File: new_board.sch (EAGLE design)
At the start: 22 parts, among them J4 455-1750-1-ND, Q1 BD437

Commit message: added analog/digital switch
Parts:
- added S4: MOMENTARY-SWITCH-SPST-SMD-RIGHT-ANGLE, SparkFun-Switches:MOMENTARY-SWITCH-SPST-SMD-RIGHT-ANGLE
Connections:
- net N$16: now also S4.1
- net N$6: now also S4.2
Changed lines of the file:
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@@
 </part>
 <part name="GND8" library="SparkFun-PowerSymbols" deviceset="GND" device=""/>
+<part name="S4" library="SparkFun-Switches" deviceset="MOMENTARY-SWITCH-SPST" device="-SMD-RIGHT-ANGLE">
+<attribute name="PROD_ID" value="Analog/Digital"/>
+</part>
 </parts>
 <sheets>
@@
 <instance part="GND8" gate="1" x="160.02" y="124.46" smashed="yes">
 <attribute name="VALUE" x="160.02" y="124.206" size="1.778" layer="96" align="top-center"/>
+</instance>
+<instance part="S4" gate="G$1" x="266.7" y="60.96" smashed="yes" rot="R90">
+<attribute name="PROD_ID" x="264.16" y="53.34" size="1.778" layer="96" rot="R90"/>
 </instance>
 </instances>
@@
 <wire x1="182.88" y1="81.28" x2="180.34" y2="81.28" width="0.1524" layer="91"/>
 <junction x="182.88" y="81.28"/>
+<pinref part="S4" gate="G$1" pin="2"/>
+<wire x1="266.7" y1="81.28" x2="266.7" y2="66.04" width="0.1524" layer="91"/>
 </segment>
 </net>
@@
 <junction x="149.86" y="76.2"/>
 <pinref part="S5" gate="G$1" pin="1"/>
-<wire x1="254" y1="20.32" x2="279.4" y2="20.32" width="0.1524" layer="91"/>
+<wire x1="254" y1="20.32" x2="266.7" y2="20.32" width="0.1524" layer="91"/>
+<wire x1="266.7" y1="20.32" x2="279.4" y2="20.32" width="0.1524" layer="91"/>
 <wire x1="279.4" y1="20.32" x2="279.4" y2="55.88" width="0.1524" layer="91"/>
 <pinref part="J4" gate="J$1" pin="3"/>
@@
 <wire x1="106.68" y1="114.3" x2="106.68" y2="76.2" width="0.1524" layer="91"/>
 <pinref part="R7" gate="G$1" pin="2"/>
-<wire x1="109.22" y1="5.08" x2="116.84" y2="5.08" width="0.1524" layer="91"/>
+<wire x1="106.68" y1="5.08" x2="116.84" y2="5.08" width="0.1524" layer="91"/>
 <wire x1="116.84" y1="5.08" x2="119.38" y2="5.08" width="0.1524" layer="91"/>
 <junction x="116.84" y="5.08"/>
 <wire x1="106.68" y1="20.32" x2="106.68" y2="5.08" width="0.1524" layer="91"/>
-<wire x1="106.68" y1="5.08" x2="109.22" y2="5.08" width="0.1524" layer="91"/>
-</segment>
-</net>
+<pinref part="S4" gate="G$1" pin="1"/>
+<wire x1="266.7" y1="55.88" x2="266.7" y2="20.32" width="0.1524" layer="91"/>
+</segment>
+</net>

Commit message: routing PCB layout
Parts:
- J2: 9V_BATTERY (none) -> 9V
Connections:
- removed net N$14: J2.2
- net GND: now also J2.2
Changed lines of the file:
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@@
 </part>
 <part name="J2" library="SparkFun-Connectors" deviceset="CONN_02" device="">
-<attribute name="9V_BATTERY" value=""/>
+<attribute name="9V_BATTERY" value="9V"/>
 </part>
 <part name="S1" library="SparkFun-Switches" deviceset="MOMENTARY-SWITCH-SPST" device="-SMD-RIGHT-ANGLE">
@@
 <attribute name="PROD_ID" value="Motor Button"/>
 </part>
-<part name="GND5" library="SparkFun-PowerSymbols" deviceset="GND" device=""/>
 <part name="J3" library="SparkFun-Connectors" deviceset="CONN_02" device="">
 <attribute name="TEAM_BATTERY" value=""/>
@@
 <instance part="S3" gate="G$1" x="269.24" y="124.46" smashed="yes" rot="R90">
 <attribute name="PROD_ID" x="266.7" y="121.92" size="1.778" layer="96" rot="R90"/>
-</instance>
-<instance part="GND5" gate="1" x="129.54" y="33.02" smashed="yes">
-<attribute name="VALUE" x="129.54" y="32.766" size="1.778" layer="96" align="top-center"/>
 </instance>
 <instance part="J3" gate="G$1" x="269.24" y="142.24" smashed="yes" rot="R270">
@@
 </segment>
 <segment>
-<pinref part="U$1" gate="G$1" pin="GND"/>
-<pinref part="GND3" gate="1" pin="GND"/>
-<wire x1="149.86" y1="71.12" x2="137.16" y2="71.12" width="0.1524" layer="91"/>
-<wire x1="137.16" y1="71.12" x2="137.16" y2="68.58" width="0.1524" layer="91"/>
-</segment>
-<segment>
 <pinref part="D5" gate="D1" pin="C"/>
 <pinref part="GND2" gate="1" pin="GND"/>
@@
 <pinref part="GND7" gate="1" pin="GND"/>
 <wire x1="139.7" y1="5.08" x2="147.32" y2="5.08" width="0.1524" layer="91"/>
+</segment>
+<segment>
+<pinref part="J2" gate="G$1" pin="2"/>
+<pinref part="U$1" gate="G$1" pin="GND"/>
+<pinref part="GND3" gate="1" pin="GND"/>
+<wire x1="149.86" y1="71.12" x2="139.7" y2="71.12" width="0.1524" layer="91"/>
+<wire x1="139.7" y1="71.12" x2="137.16" y2="71.12" width="0.1524" layer="91"/>
+<wire x1="137.16" y1="71.12" x2="137.16" y2="68.58" width="0.1524" layer="91"/>
+<wire x1="139.7" y1="38.1" x2="139.7" y2="71.12" width="0.1524" layer="91"/>
 </segment>
 </net>
@@
 </segment>
 </net>
-<net name="N$14" class="0">
-<segment>
-<pinref part="J2" gate="G$1" pin="2"/>
-<wire x1="139.7" y1="38.1" x2="139.7" y2="40.64" width="0.1524" layer="91"/>
-<wire x1="139.7" y1="40.64" x2="129.54" y2="40.64" width="0.1524" layer="91"/>
-<wire x1="129.54" y1="40.64" x2="129.54" y2="35.56" width="0.1524" layer="91"/>
-<pinref part="GND5" gate="1" pin="GND"/>
-<wire x1="129.54" y1="35.56" x2="129.54" y2="33.02" width="0.1524" layer="91"/>
-<junction x="129.54" y="35.56"/>
-</segment>
-</net>

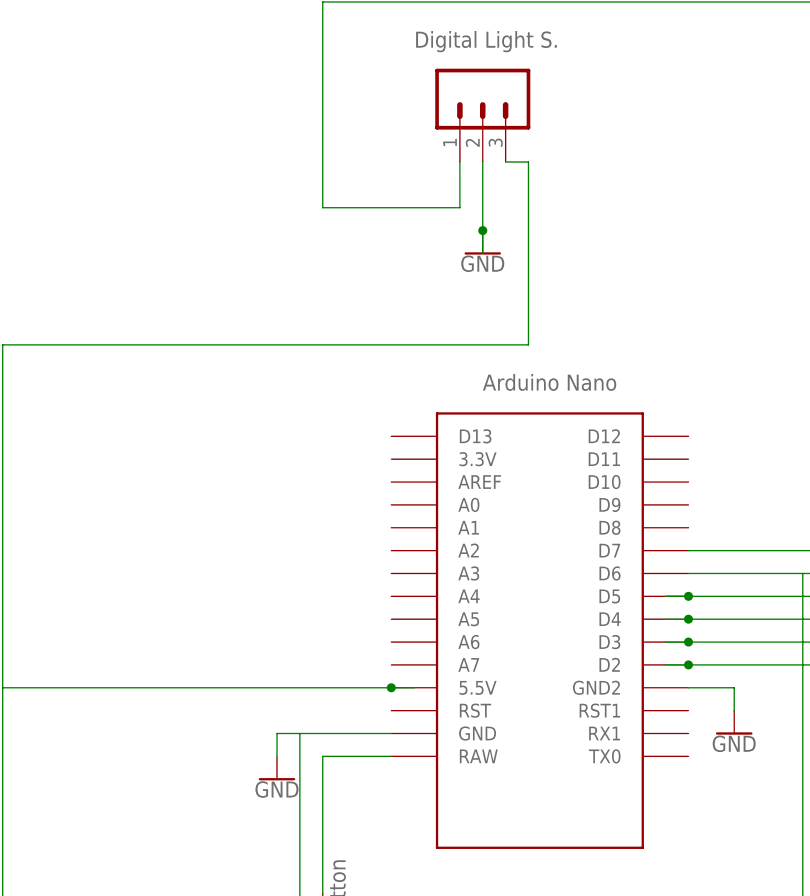
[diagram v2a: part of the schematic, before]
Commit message: finished labeling signals and buttons
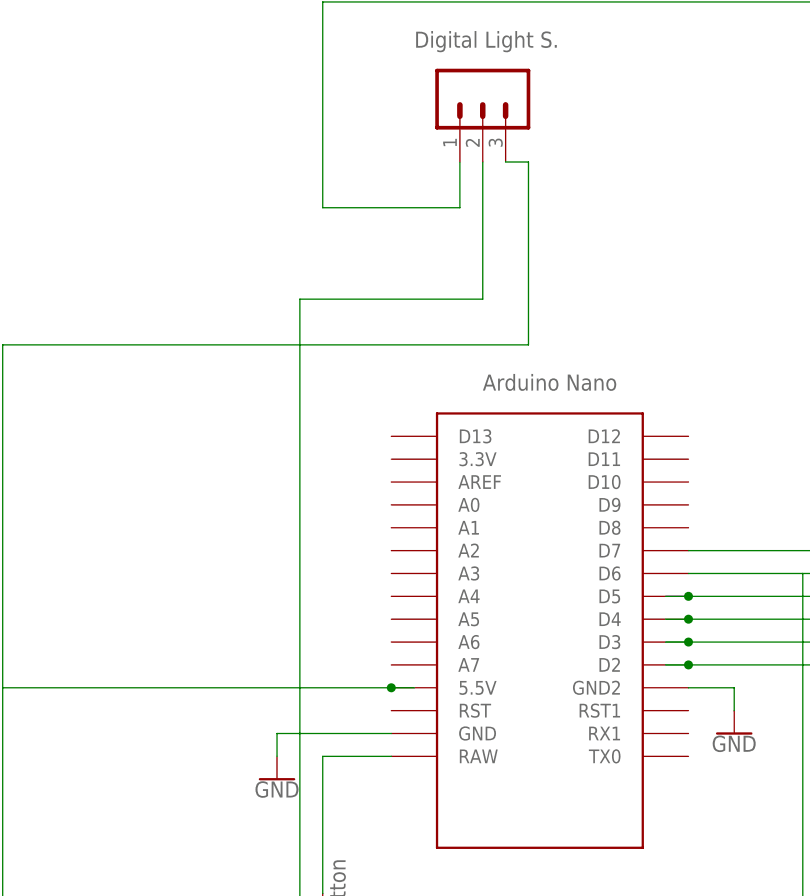
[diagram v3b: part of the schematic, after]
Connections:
- removed net N$18: J4.2
- net GND: now also J4.2
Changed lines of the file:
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@@
 <attribute name="PROD_ID" value="Digital Light S."/>
 </part>
-<part name="GND8" library="SparkFun-PowerSymbols" deviceset="GND" device=""/>
 <part name="S4" library="SparkFun-Switches" deviceset="MOMENTARY-SWITCH-SPST" device="-SMD-RIGHT-ANGLE">
 <attribute name="PROD_ID" value="Analog/Digital"/>
@@
 <instance part="J4" gate="J$1" x="160.02" y="142.24" smashed="yes" rot="R270">
 <attribute name="PROD_ID" x="152.4" y="147.32" size="1.778" layer="96"/>
-</instance>
-<instance part="GND8" gate="1" x="160.02" y="124.46" smashed="yes">
-<attribute name="VALUE" x="160.02" y="124.206" size="1.778" layer="96" align="top-center"/>
 </instance>
 <instance part="S4" gate="G$1" x="266.7" y="60.96" smashed="yes" rot="R90">
@@
 <wire x1="137.16" y1="71.12" x2="137.16" y2="68.58" width="0.1524" layer="91"/>
 <wire x1="139.7" y1="38.1" x2="139.7" y2="71.12" width="0.1524" layer="91"/>
+<pinref part="J4" gate="J$1" pin="2"/>
+<wire x1="160.02" y1="134.62" x2="160.02" y2="119.38" width="0.1524" layer="91"/>
+<wire x1="160.02" y1="119.38" x2="139.7" y2="119.38" width="0.1524" layer="91"/>
+<wire x1="139.7" y1="119.38" x2="139.7" y2="71.12" width="0.1524" layer="91"/>
 </segment>
 </net>
@@
 </segment>
 </net>
-<net name="N$18" class="0">
-<segment>
-<pinref part="J4" gate="J$1" pin="2"/>
-<wire x1="160.02" y1="134.62" x2="160.02" y2="127" width="0.1524" layer="91"/>
-<pinref part="GND8" gate="1" pin="GND"/>
-<wire x1="160.02" y1="127" x2="160.02" y2="124.46" width="0.1524" layer="91"/>
-<junction x="160.02" y="127"/>
-</segment>
-</net>

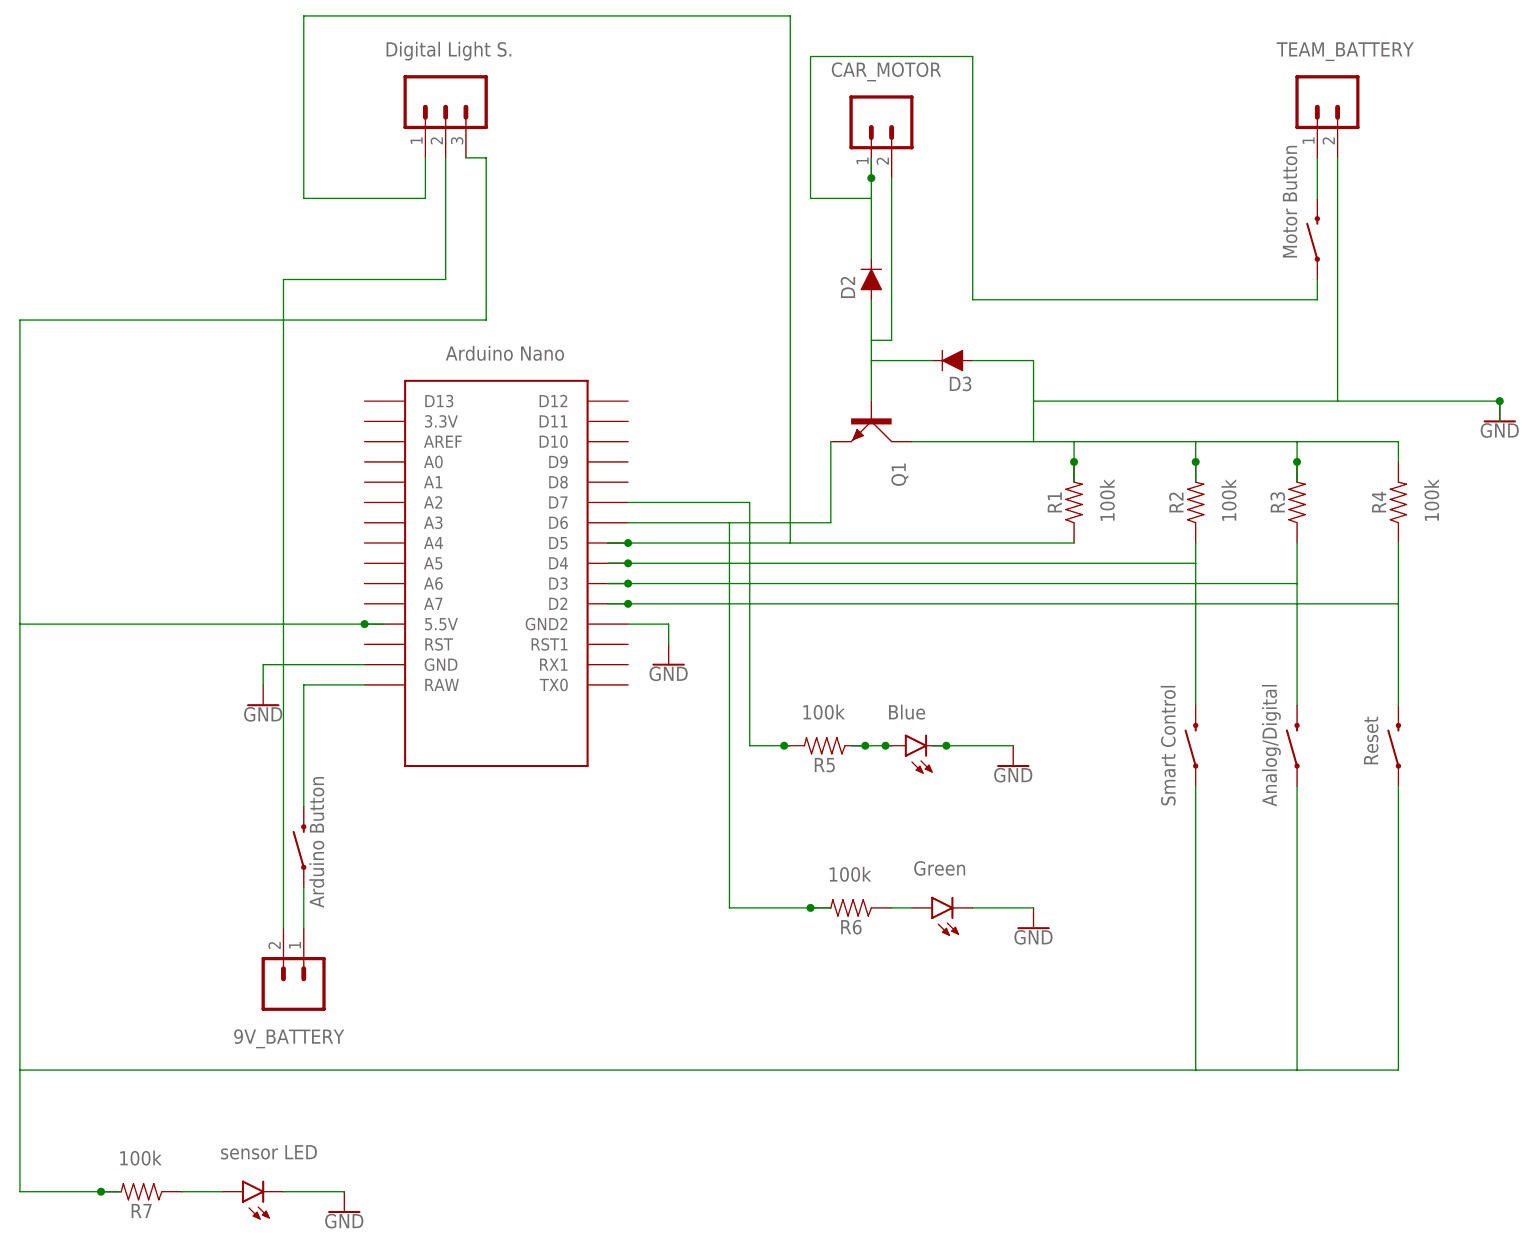
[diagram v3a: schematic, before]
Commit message: switched out switches for through-holes
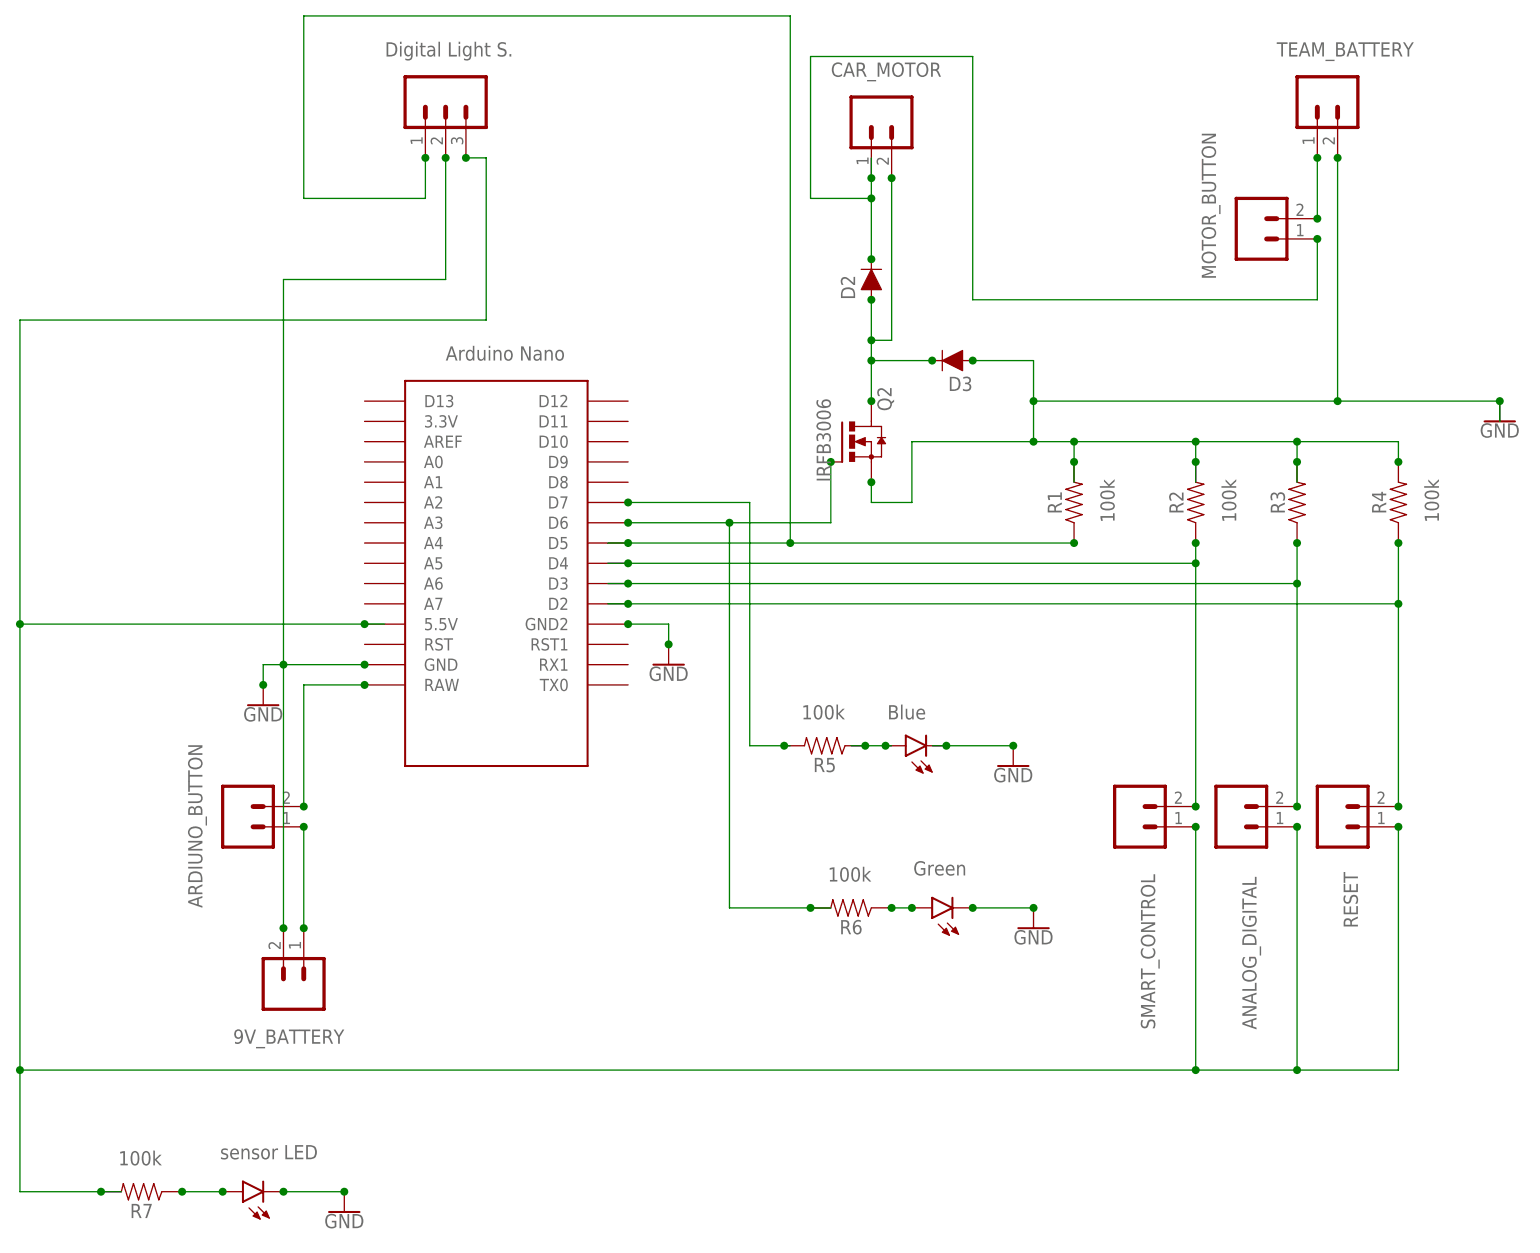
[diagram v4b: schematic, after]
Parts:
- removed Q1: BD437, transistor-power:BD437
- added Q2: IRF3704L-V, transistor-power:IRF3704L-V
- S1: value MOMENTARY-SWITCH-SPST-SMD-RIGHT-ANGLE -> (none); device SparkFun-Switches:MOMENTARY-SWITCH-SPST-SMD-RIGHT-ANGLE -> SparkFun-Connectors:CONN_02; PROD_ID Arduino Button -> (none)
- S2: value MOMENTARY-SWITCH-SPST-SMD-RIGHT-ANGLE -> (none); device SparkFun-Switches:MOMENTARY-SWITCH-SPST-SMD-RIGHT-ANGLE -> SparkFun-Connectors:CONN_02; PROD_ID Smart Control -> (none)
- S3: value MOMENTARY-SWITCH-SPST-SMD-RIGHT-ANGLE -> (none); device SparkFun-Switches:MOMENTARY-SWITCH-SPST-SMD-RIGHT-ANGLE -> SparkFun-Connectors:CONN_02; PROD_ID Motor Button -> (none)
- S4: value MOMENTARY-SWITCH-SPST-SMD-RIGHT-ANGLE -> (none); device SparkFun-Switches:MOMENTARY-SWITCH-SPST-SMD-RIGHT-ANGLE -> SparkFun-Connectors:CONN_02; PROD_ID Analog/Digital -> (none)
- S5: value MOMENTARY-SWITCH-SPST-SMD-RIGHT-ANGLE -> (none); device SparkFun-Switches:MOMENTARY-SWITCH-SPST-SMD-RIGHT-ANGLE -> SparkFun-Connectors:CONN_02; PROD_ID Reset -> (none)
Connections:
- net N$1: now also Q2.G; no longer Q1.E
- net N$2: now also Q2.D; no longer Q1.B
- net N$3: now also Q2.S; no longer Q1.C

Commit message: added ground and power planes, and changed resistor values/added resistor after the mosfet gate
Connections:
- net N$16 renamed 5V
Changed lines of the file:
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@@
 </segment>
 </net>
-<net name="N$16" class="0">
+<net name="5V" class="0">
 <segment>
 <pinref part="S2" gate="G$1" pin="1"/>
